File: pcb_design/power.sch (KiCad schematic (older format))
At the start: 35 parts, among them Q1 BSC340N08, U11 LM3488, U13 LM1117IMP-v.v, U9 LM22676QTJ-5.0

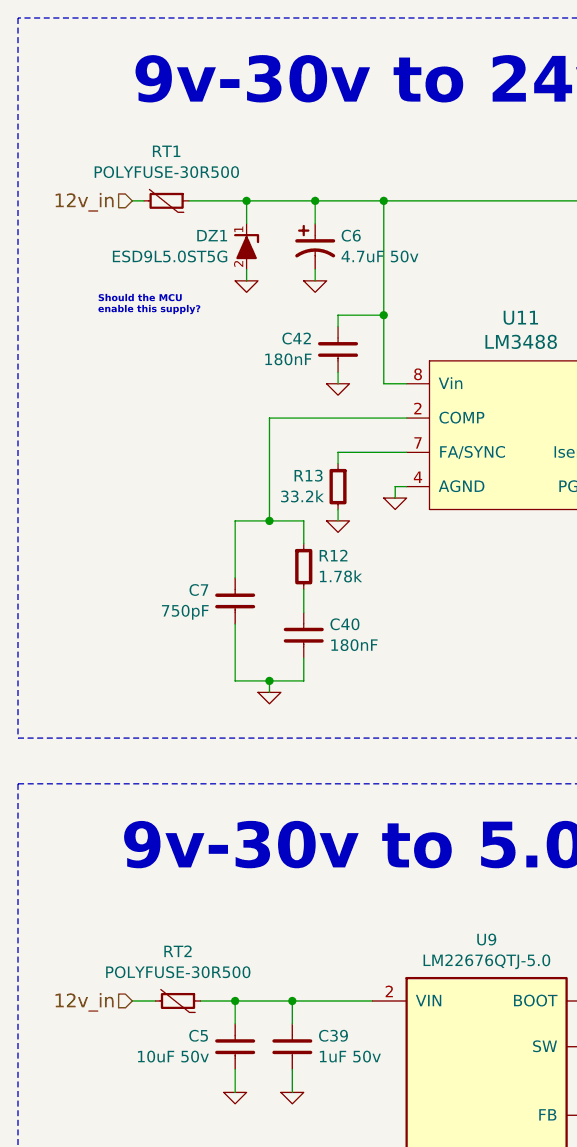
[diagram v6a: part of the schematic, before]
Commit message: More layout. Changed LED pin. Added placeholder for a resolver IC
Signed-off-by: Marcos Chaparro <mchaparro@paltatech.com>
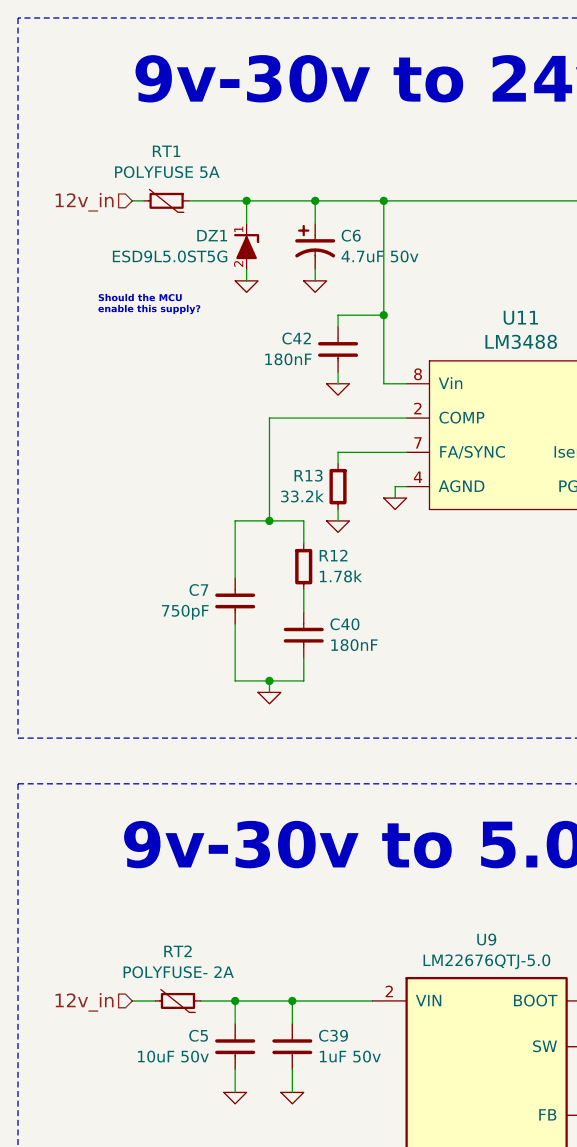
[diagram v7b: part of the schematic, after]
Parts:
- RT1: value POLYFUSE-30R500 -> POLYFUSE 5A
- RT2: value POLYFUSE-30R500 -> POLYFUSE- 2A
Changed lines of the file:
@@
 $Descr A4 11693 8268
 encoding utf-8
-Sheet 6 13
+Sheet 6 14
 Title "Power supplies"
 Date "2017-01-24"
@@
 Connection ~ 2100 4150
 $Comp
-L GND #PWR62
+L GND #PWR060
 U 1 1 588BC982
 P 2100 4200
-F 0 "#PWR62" H 2100 4200 30  0001 C CNN
+F 0 "#PWR060" H 2100 4200 30  0001 C CNN
 F 1 "GND" H 2100 4130 30  0001 C CNN
 F 2 "" H 2100 4200 60  0000 C CNN
@@
 	2400 3150 2400 3200
 $Comp
-L GND #PWR66
+L GND #PWR061
 U 1 1 588BD2D9
 P 2400 3450
-F 0 "#PWR66" H 2400 3450 30  0001 C CNN
+F 0 "#PWR061" H 2400 3450 30  0001 C CNN
 F 1 "GND" H 2400 3380 30  0001 C CNN
 F 2 "" H 2400 3450 60  0000 C CNN
@@
 	2400 3450 2400 3400
 $Comp
-L GND #PWR67
+L GND #PWR062
 U 1 1 588BD345
 P 2650 3350
-F 0 "#PWR67" H 2650 3350 30  0001 C CNN
+F 0 "#PWR062" H 2650 3350 30  0001 C CNN
 F 1 "GND" H 2650 3280 30  0001 C CNN
 F 2 "" H 2650 3350 60  0000 C CNN
@@
 	3750 3300 3750 3350
 $Comp
-L GND #PWR69
+L GND #PWR063
 U 1 1 588BD634
 P 3750 3350
-F 0 "#PWR69" H 3750 3350 30  0001 C CNN
+F 0 "#PWR063" H 3750 3350 30  0001 C CNN
 F 1 "GND" H 3750 3280 30  0001 C CNN
 F 2 "" H 3750 3350 60  0000 C CNN
@@
 	4050 3550 4050 3600
 $Comp
-L GND #PWR70
+L GND #PWR064
 U 1 1 588BDA1B
 P 4050 3600
-F 0 "#PWR70" H 4050 3600 30  0001 C CNN
+F 0 "#PWR064" H 4050 3600 30  0001 C CNN
 F 1 "GND" H 4050 3530 30  0001 C CNN
 F 2 "" H 4050 3600 60  0000 C CNN
@@
 	4600 3550 4600 3600
 $Comp
-L GND #PWR72
+L GND #PWR065
 U 1 1 588BDE06
 P 4600 3600
-F 0 "#PWR72" H 4600 3600 30  0001 C CNN
+F 0 "#PWR065" H 4600 3600 30  0001 C CNN
 F 1 "GND" H 4600 3530 30  0001 C CNN
 F 2 "" H 4600 3600 60  0000 C CNN
@@
 Connection ~ 2600 2550
 $Comp
-L GND #PWR65
+L GND #PWR066
 U 1 1 588BFA6D
 P 2400 2850
-F 0 "#PWR65" H 2400 2850 30  0001 C CNN
+F 0 "#PWR066" H 2400 2850 30  0001 C CNN
 F 1 "GND" H 2400 2780 30  0001 C CNN
 F 2 "" H 2400 2850 60  0000 C CNN
@@
 	2300 2150 2300 2050
 $Comp
-L GND #PWR64
+L GND #PWR067
 U 1 1 588C0261
 P 2300 2400
-F 0 "#PWR64" H 2300 2400 30  0001 C CNN
+F 0 "#PWR067" H 2300 2400 30  0001 C CNN
 F 1 "GND" H 2300 2330 30  0001 C CNN
 F 2 "" H 2300 2400 60  0000 C CNN
@@
 	5150 2050 5850 2050
 $Comp
-L GND #PWR74
+L GND #PWR068
 U 1 1 588C0D64
 P 5400 2500
-F 0 "#PWR74" H 5400 2500 30  0001 C CNN
+F 0 "#PWR068" H 5400 2500 30  0001 C CNN
 F 1 "GND" H 5400 2430 30  0001 C CNN
 F 2 "" H 5400 2500 60  0000 C CNN
@@
 	6050 2050 7300 2050
 $Comp
-L GND #PWR77
+L GND #PWR069
 U 1 1 588C18FD
 P 6250 3050
-F 0 "#PWR77" H 6250 3050 30  0001 C CNN
+F 0 "#PWR069" H 6250 3050 30  0001 C CNN
 F 1 "GND" H 6250 2980 30  0001 C CNN
 F 2 "" H 6250 3050 60  0000 C CNN
@@
 Connection ~ 6850 2050
 $Comp
-L GND #PWR78
+L GND #PWR070
 U 1 1 588C2312
 P 6850 2500
-F 0 "#PWR78" H 6850 2500 30  0001 C CNN
+F 0 "#PWR070" H 6850 2500 30  0001 C CNN
 F 1 "GND" H 6850 2430 30  0001 C CNN
 F 2 "" H 6850 2500 60  0000 C CNN
@@
 	6850 2500 6850 2400
 $Comp
-L GND #PWR80
+L GND #PWR071
 U 1 1 588C2433
 P 7050 2500
-F 0 "#PWR80" H 7050 2500 30  0001 C CNN
+F 0 "#PWR071" H 7050 2500 30  0001 C CNN
 F 1 "GND" H 7050 2430 30  0001 C CNN
 F 2 "" H 7050 2500 60  0000 C CNN
@@
 Connection ~ 2200 5550
 $Comp
-L GND #PWR60
+L GND #PWR072
 U 1 1 588C4382
 P 1950 5950
-F 0 "#PWR60" H 1950 5950 30  0001 C CNN
+F 0 "#PWR072" H 1950 5950 30  0001 C CNN
 F 1 "GND" H 1950 5880 30  0001 C CNN
 F 2 "" H 1950 5950 60  0000 C CNN
@@
 	1950 5950 1950 5850
 $Comp
-L GND #PWR63
+L GND #PWR073
 U 1 1 588C4468
 P 2200 5950
-F 0 "#PWR63" H 2200 5950 30  0001 C CNN
+F 0 "#PWR073" H 2200 5950 30  0001 C CNN
 F 1 "GND" H 2200 5880 30  0001 C CNN
 F 2 "" H 2200 5950 60  0000 C CNN
@@
 Connection ~ 4000 5750
 $Comp
-L GND #PWR71
+L GND #PWR074
 U 1 1 588C56F7
 P 4100 6050
-F 0 "#PWR71" H 4100 6050 30  0001 C CNN
+F 0 "#PWR074" H 4100 6050 30  0001 C CNN
 F 1 "GND" H 4100 5980 30  0001 C CNN
 F 2 "" H 4100 6050 60  0000 C CNN
@@
 Connection ~ 5300 5750
 $Comp
-L GND #PWR73
+L GND #PWR075
 U 1 1 588C63EB
 P 5300 6250
-F 0 "#PWR73" H 5300 6250 30  0001 C CNN
+F 0 "#PWR075" H 5300 6250 30  0001 C CNN
 F 1 "GND" H 5300 6180 30  0001 C CNN
 F 2 "" H 5300 6250 60  0000 C CNN
@@
 $EndComp
 $Comp
-L GND #PWR75
+L GND #PWR076
 U 1 1 588C6447
 P 5550 6250
-F 0 "#PWR75" H 5550 6250 30  0001 C CNN
+F 0 "#PWR076" H 5550 6250 30  0001 C CNN
 F 1 "GND" H 5550 6180 30  0001 C CNN
 F 2 "" H 5550 6250 60  0000 C CNN
@@
 NoConn ~ 2550 6350
 $Comp
-L GND #PWR68
+L GND #PWR077
 U 1 1 588C6DC2
 P 3650 6450
-F 0 "#PWR68" H 3650 6450 30  0001 C CNN
+F 0 "#PWR077" H 3650 6450 30  0001 C CNN
 F 1 "GND" H 3650 6380 30  0001 C CNN
 F 2 "" H 3650 6450 60  0000 C CNN
@@
 Connection ~ 7000 5750
 $Comp
-L GND #PWR79
+L GND #PWR078
 U 1 1 588C792B
 P 7000 6250
-F 0 "#PWR79" H 7000 6250 30  0001 C CNN
+F 0 "#PWR078" H 7000 6250 30  0001 C CNN
 F 1 "GND" H 7000 6180 30  0001 C CNN
 F 2 "" H 7000 6250 60  0000 C CNN
@@
 	7000 6250 7000 6150
 $Comp
-L GND #PWR82
+L GND #PWR079
 U 1 1 588C79EC
 P 7500 6150
-F 0 "#PWR82" H 7500 6150 30  0001 C CNN
+F 0 "#PWR079" H 7500 6150 30  0001 C CNN
 F 1 "GND" H 7500 6080 30  0001 C CNN
 F 2 "" H 7500 6150 60  0000 C CNN
@@
 Connection ~ 8050 5750
 $Comp
-L GND #PWR83
+L GND #PWR080
 U 1 1 588C813C
 P 8050 6250
-F 0 "#PWR83" H 8050 6250 30  0001 C CNN
+F 0 "#PWR080" H 8050 6250 30  0001 C CNN
 F 1 "GND" H 8050 6180 30  0001 C CNN
 F 2 "" H 8050 6250 60  0000 C CNN
@@
 	8050 6250 8050 6150
 $Comp
-L GND #PWR84
+L GND #PWR081
 U 1 1 588C81BF
 P 8250 6250
-F 0 "#PWR84" H 8250 6250 30  0001 C CNN
+F 0 "#PWR081" H 8250 6250 30  0001 C CNN
 F 1 "GND" H 8250 6180 30  0001 C CNN
 F 2 "" H 8250 6250 60  0000 C CNN
@@
 	9750 4600 6400 4600
 $Comp
-L +3.3 #PWR85
+L +3.3 #PWR082
 U 1 1 588BD2B2
 P 8450 5750
-F 0 "#PWR85" H 8500 5800 30  0001 C CNN
+F 0 "#PWR082" H 8500 5800 30  0001 C CNN
 F 1 "+3.3" H 8450 5883 50  0000 C CNN
 F 2 "" H -100 0   60  0000 C CNN
@@
 $EndComp
 $Comp
-L +5 #PWR76
+L +5 #PWR083
 U 1 1 588BD705
 P 5650 5700
-F 0 "#PWR76" H 5700 5750 30  0001 C CNN
+F 0 "#PWR083" H 5700 5750 30  0001 C CNN
 F 1 "+5" H 5650 5833 50  0000 C CNN
 F 2 "" H -400 50  60  0000 C CNN
@@
 P 1650 2050
 F 0 "RT1" V 1435 2050 50  0000 C CNN
-F 1 "POLYFUSE-30R500" V 1526 2050 50  0000 C CNN
+F 1 "POLYFUSE 5A" V 1526 2050 50  0000 C CNN
 F 2 "IPC7351-Most:RESC3216X60" H 150 -1000 60  0001 C CNN
 F 3 "" H 150 -1100 60  0000 C CNN
@@
 Connection ~ 2000 2050
 $Comp
-L GND #PWR61
+L GND #PWR084
 U 1 1 588CB9A0
 P 2000 2400
-F 0 "#PWR61" H 2000 2400 30  0001 C CNN
+F 0 "#PWR084" H 2000 2400 30  0001 C CNN
 F 1 "GND" H 2000 2330 30  0001 C CNN
 F 2 "" H 2000 2400 60  0000 C CNN
@@
 P 1700 5550
 F 0 "RT2" V 1485 5550 50  0000 C CNN
-F 1 "POLYFUSE-30R500" V 1576 5550 50  0000 C CNN
+F 1 "POLYFUSE- 2A" V 1576 5550 50  0000 C CNN
 F 2 "IPC7351-Most:RESC3216X60" H 200 2500 60  0001 C CNN
 F 3 "" H 200 2400 60  0000 C CNN
@@
 Connection ~ 7050 5750
 $Comp
-L +24 #PWR81
+L +24 #PWR085
 U 1 1 588CFB19
 P 7300 2050
-F 0 "#PWR81" H -100 50  30  0001 C CNN
+F 0 "#PWR085" H -100 50  30  0001 C CNN
 F 1 "+24" H 7300 2183 50  0000 C CNN
 F 2 "" H -100 0   60  0000 C CNN
